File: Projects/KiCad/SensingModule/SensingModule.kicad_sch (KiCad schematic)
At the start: 18 parts, among them J1 Conn_01x04_Pin, J2 Conn_01x04_Socket, J3 Micro_SD_Card_Det_Hirose_DM3AT, U1 NUCLEO-F303K8, U2 MCP2562-E-P, U3 24LC256

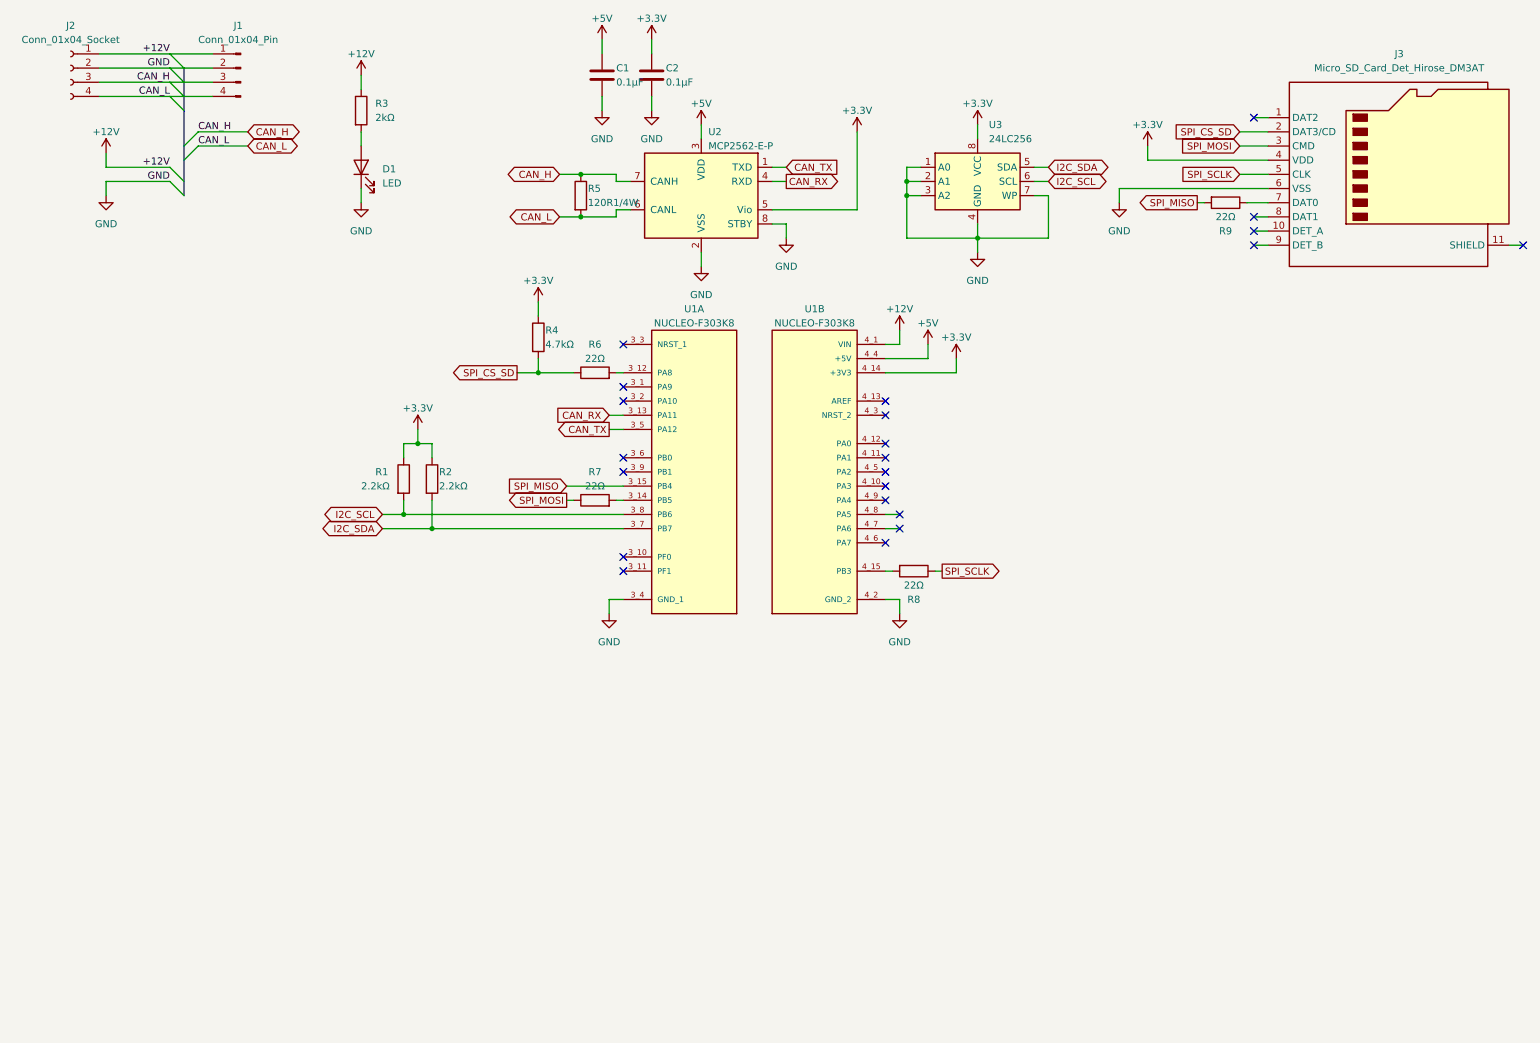
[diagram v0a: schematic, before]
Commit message: 通信モジュールを一旦作成
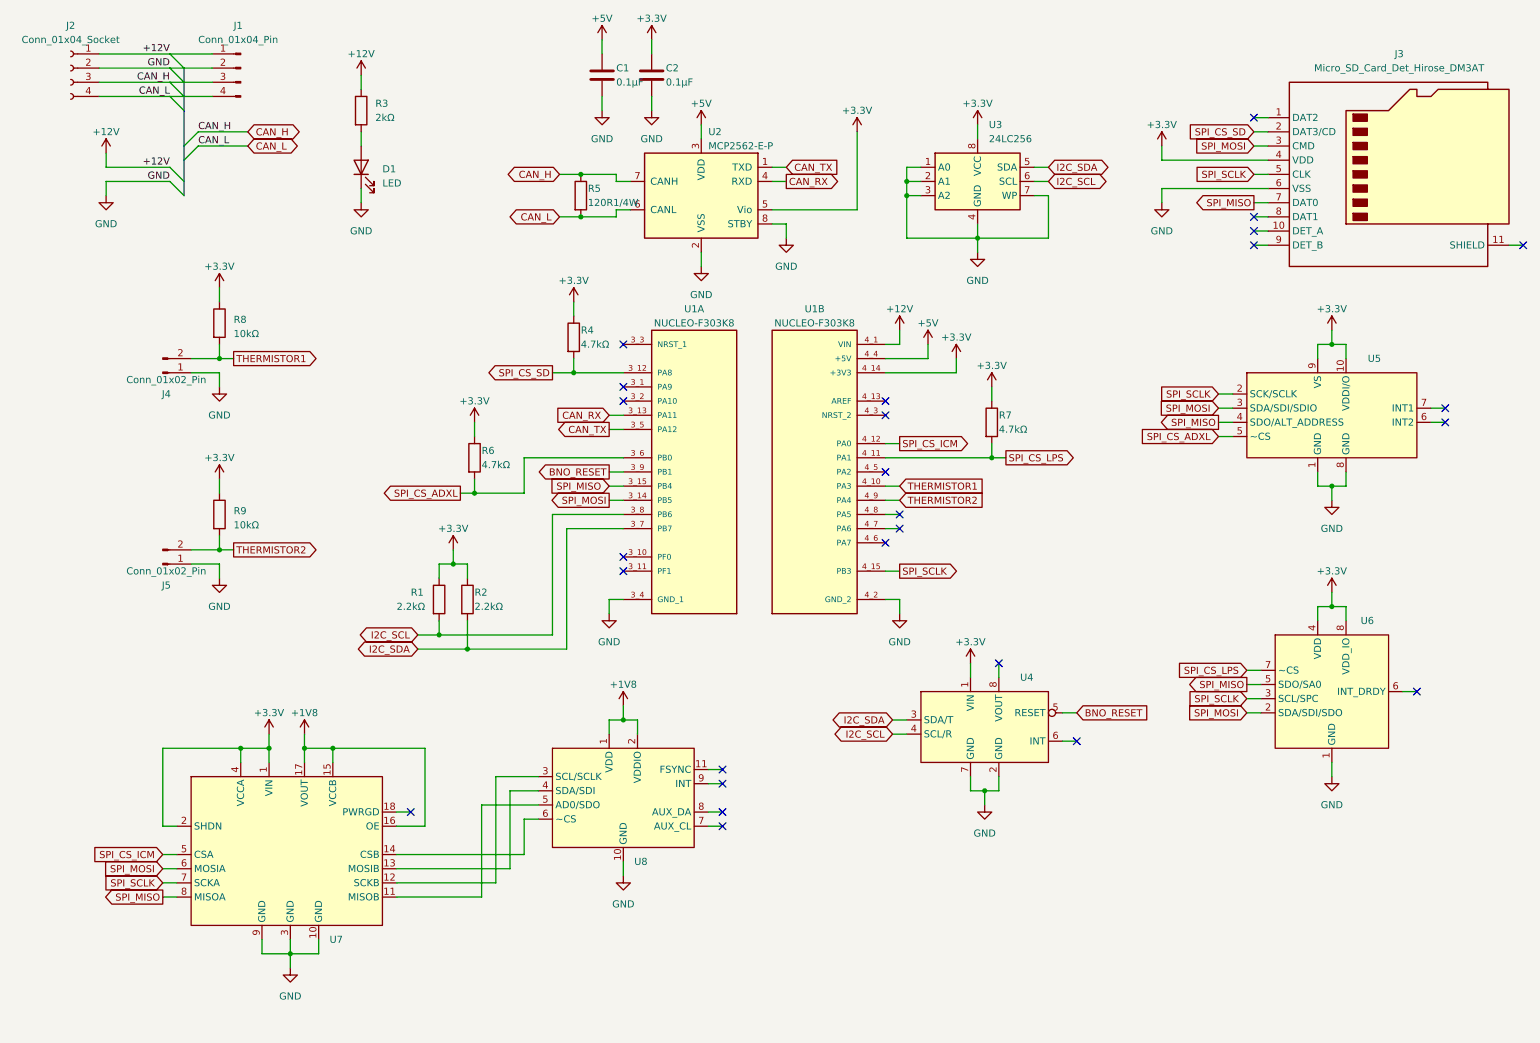
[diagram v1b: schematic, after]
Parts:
- added J4, J5: Conn_01x02_Pin, Hirose_Connector:Hirose_DF1B, symbol Connector:Conn_01x02_Pin
- added U4: ~, Akizuki_BNO055_Module:BNO055, symbol Akizuki_BNO055_Module:BNO055
- added U5: ~, StrawberryLinux_ADXL375_Module:ADXL375, symbol StrawberryLinux_ADXL375_Module:ADXL375
- added U6: ~, StrawberryLinux_LPS33HW_Module:LPS33HW, symbol StrawberryLinux_LPS33HW_Module:LPS33HW
- added U7: ~, StrawberryLinux_TUX0304_Module:TUX0304, symbol StrawberryLinux_TUX0304_Module:TUX0304
- added U8: ~, StrawberryLinux_ICM20948_Module:ICM20948, symbol StrawberryLinux_ICM20948_Module:ICM20948
- R6, R7: value 22Ω -> 4.7kΩ
- R8, R9: value 22Ω -> 10kΩ
- U1: footprint MODULE_NUCLEO-F303K8 -> NUCLEO-F303K8:MODULE_NUCLEO-F303K8
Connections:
- net +3.3V: now also R6.1, R7.1, R8.1, R9.1, U4.1 (VIN), U5.10 (VDDI/O), U5.9 (VS), U6.4 (VDD), U6.8 (VDD_IO), U7.1 (VIN), U7.2 (SHDN), U7.4 (VCCA)
- net GND: now also J4.1 (Pin_1), J5.1 (Pin_1), U4.2 (GND), U4.7 (GND), U5.1 (GND), U5.8 (GND), U6.1 (GND), U7.10 (GND), U7.3 (GND), U7.9 (GND), U8.10 (GND)
- net I2C_SCL: now also U4.4 (SCL/R)
- net I2C_SDA: now also U4.3 (SDA/T)
- net SPI_CS_SD: now also U1.3_12 (PA8); no longer R6.1
- net SPI_MISO: now also J3.7 (DAT0), U5.4 (SDO/ALT_ADDRESS), U6.5 (SDO/SA0), U7.8 (MISOA); no longer R9.2
- net SPI_MOSI: now also U1.3_14 (PB5), U5.3 (SDA/SDI/SDIO), U6.2 (SDA/SDI/SDO), U7.6 (MOSIA); no longer R7.1
- net SPI_SCLK: now also U1.4_15 (PB3), U5.2 (SCK/SCLK), U6.3 (SCL/SPC), U7.7 (SCKA); no longer R8.1
- net SPI_CS_ADXL: now reaches R6.2
- net SPI_CS_ADXL: now also U1.3_6 (PB0), U5.5 (~CS); no longer U1.3_12 (PA8)
- net THERMISTOR1: now reaches R8.2
- net THERMISTOR1: now also U1.4_10 (PA3), J4.2 (Pin_2); no longer U1.4_15 (PB3)
- net SPI_CS_LPS: now reaches R7.2
- net SPI_CS_LPS: now also U1.4_11 (PA1), U6.7 (~CS); no longer U1.3_14 (PB5)
- net SPI_CS_ICM: now reaches U1.4_12 (PA0)
- net SPI_CS_ICM: now also U7.5 (CSA)
- net THERMISTOR2: now reaches U1.4_9 (PA4)
- net THERMISTOR2: now also R9.2, J5.2 (Pin_2)
- net BNO_RESET: now reaches U1.3_9 (PB1)
- net BNO_RESET: now also U4.5 (RESET)
- new net: U7.12 (SCKB), U8.3 (SCL/SCLK)
- new net: U7.13 (MOSIB), U8.4 (SDA/SDI)
- new net: U7.11 (MISOB), U8.5 (AD0/SDO)
- new net: U7.14 (CSB), U8.6 (~CS)
- new net +1V8: U7.15 (VCCB), U7.16 (OE), U7.17 (VOUT), U8.1 (VDD), U8.2 (VDDIO)
- no-connect marks 22 -> 26
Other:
- moved on the sheet: R1, R2, R4

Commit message: フライトモジュールのKiCadを追加
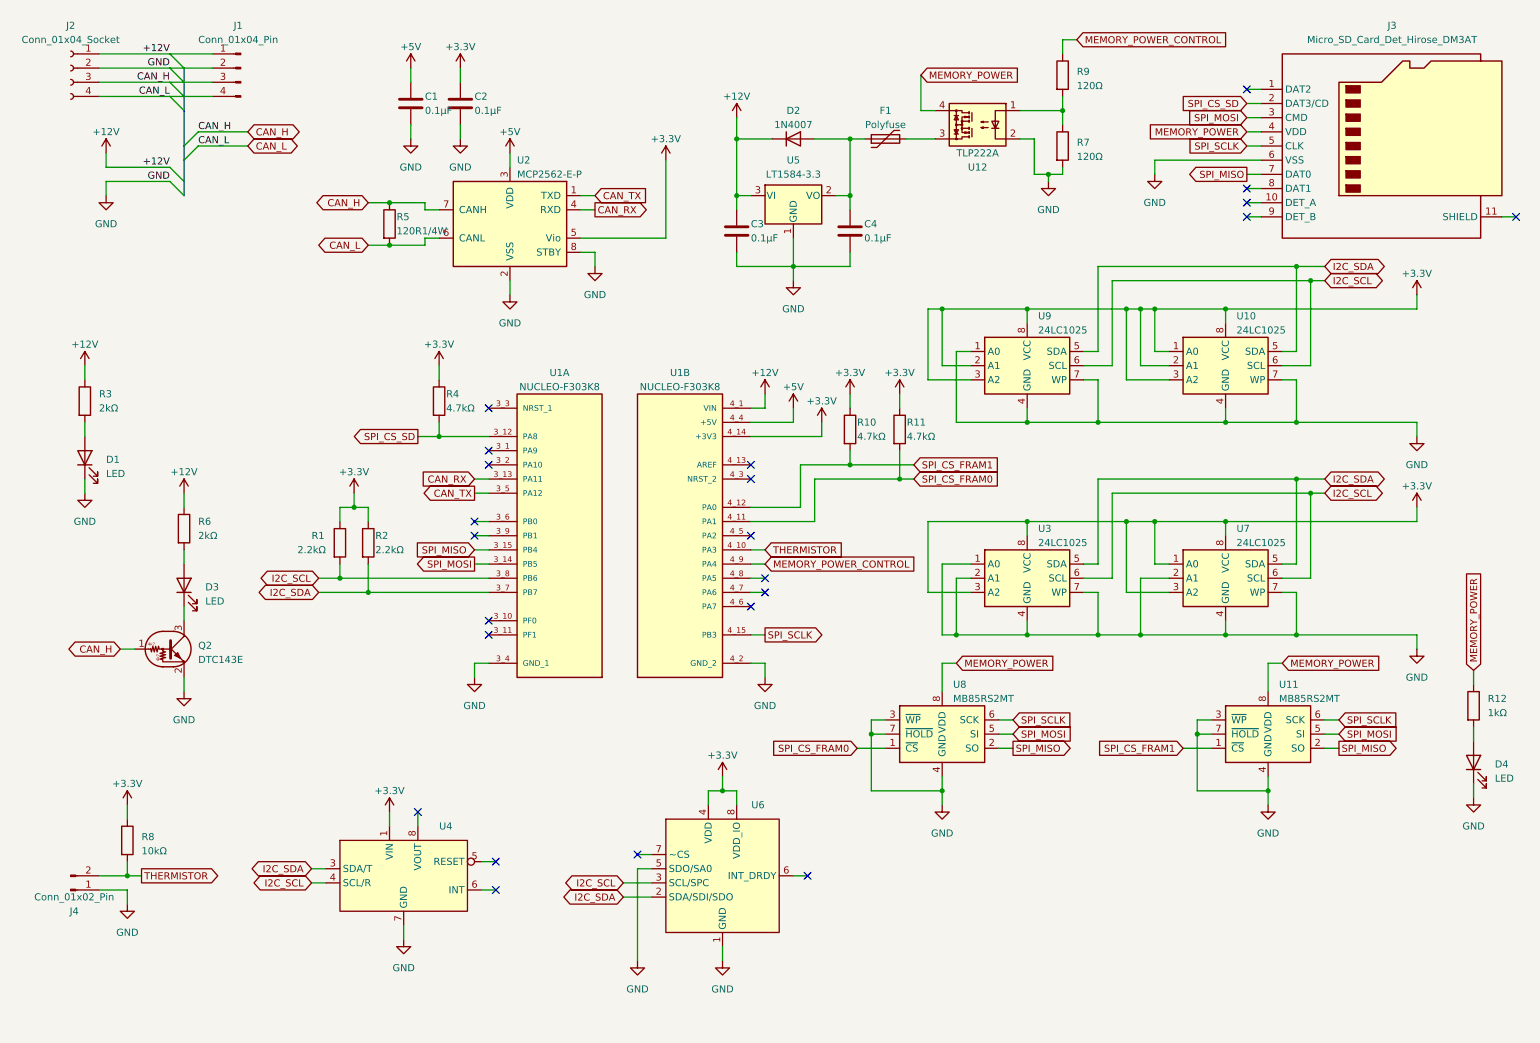
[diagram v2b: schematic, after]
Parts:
- removed J5: Conn_01x02_Pin, Hirose_Connector:Hirose_DF1B, symbol Connector:Conn_01x02_Pin
- removed U3: 24LC256, Package_DIP:DIP-8_W7.62mm, symbol Memory_EEPROM:24LC256
- removed U5: ~, StrawberryLinux_ADXL375_Module:ADXL375, symbol StrawberryLinux_ADXL375_Module:ADXL375
- removed U7: ~, StrawberryLinux_TUX0304_Module:TUX0304, symbol StrawberryLinux_TUX0304_Module:TUX0304
- removed U8: ~, StrawberryLinux_ICM20948_Module:ICM20948, symbol StrawberryLinux_ICM20948_Module:ICM20948
- added C3, C4: 0.1μF, Capacitor_SMD:C_0805_2012Metric_Pad1.18x1.45mm_HandSolder, symbol Device:C
- added D2: 1N4007, Diode_THT:D_DO-41_SOD81_P10.16mm_Horizontal, symbol Diode:1N4007
- added D3, D4: LED, LED_SMD:LED_1206_3216Metric_Pad1.42x1.75mm_HandSolder, symbol Device:LED
- added F1: Polyfuse, Fuse:Fuse_BelFuse_0ZRE0005FF_L8.3mm_W3.8mm, symbol Device:Polyfuse
- added Q2: DTC143E, Package_TO_SOT_THT:TO-92_Inline, symbol Transistor_BJT:DTC143E
- added R10, R11: 4.7kΩ, Resistor_SMD:R_0805_2012Metric_Pad1.20x1.40mm_HandSolder, symbol Device:R
- added R12: 1kΩ, Resistor_SMD:R_0805_2012Metric_Pad1.20x1.40mm_HandSolder, symbol Device:R
- added U10, U3, U7, U9: 24LC1025, Package_DIP:DIP-8_W7.62mm, symbol Memory_EEPROM:24LC1025
- added U11, U8: MB85RS2MT, Package_DIP:DIP-8_W7.62mm, symbol Memory_NVRAM:MB85RS2MT
- added U12: TLP222A, Package_DIP:DIP-4_W7.62mm, symbol Relay_SolidState:TLP222A
- added U5: LT1584-3.3, Package_TO_SOT_THT:TO-220-3_Vertical, symbol Regulator_Linear:LT1584-3.3
- R6: value 4.7kΩ -> 2kΩ
- R7: value 4.7kΩ -> 120Ω
- R9: value 10kΩ -> 120Ω
- U1: footprint NUCLEO-F303K8:MODULE_NUCLEO-F303K8 -> MODULE_NUCLEO-F303K8
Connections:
- net +12V: now also R6.1, C3.1, D2.1 (K), U5.3 (VI)
- net +3.3V: now also R10.1, R11.1, U10.1 (A0), U10.2 (A1), U10.3 (A2), U10.8 (VCC), U3.3 (A2), U3.8 (VCC), U7.1 (A0), U7.3 (A2), U7.8 (VCC), U9.2 (A1), U9.3 (A2), U9.8 (VCC); no longer J3.4 (VDD), R6.1, R7.1, R9.1
- net CAN_H: now also Q2.1 (B)
- net GND: now also R7.2, U6.5 (SDO/SA0), C3.2, C4.2, D4.1 (K), Q2.2 (E), U10.4 (GND), U10.7 (WP), U11.3 (~{WP}), U11.4 (GND), U11.7 (~{HOLD}), U12.2, U3.1 (A0), U3.2 (A1), U3.4 (GND), U3.7 (WP), U5.1 (GND), U7.2 (A1), U7.4 (GND), U7.7 (WP), U8.3 (~{WP}), U8.4 (GND), U8.7 (~{HOLD}), U9.1 (A0), U9.4 (GND), U9.7 (WP); no longer U4.2 (GND)
- net I2C_SCL: now also U6.3 (SCL/SPC), U10.6 (SCL), U3.6 (SCL), U7.6 (SCL), U9.6 (SCL)
- net I2C_SDA: now also U6.2 (SDA/SDI/SDO), U10.5 (SDA), U3.5 (SDA), U7.5 (SDA), U9.5 (SDA)
- net SPI_MISO: now also U11.2 (SO), U8.2 (SO); no longer U6.5 (SDO/SA0)
- net SPI_MOSI: now also U11.5 (SI), U8.5 (SI); no longer U6.2 (SDA/SDI/SDO)
- net SPI_SCLK: now also U11.6 (SCK), U8.6 (SCK); no longer U6.3 (SCL/SPC)
- net BNO_RESET: no longer names the net of U4.5 (RESET)
- net BNO_RESET: no longer U1.3_9 (PB1)
- net SPI_CS_ADXL: no longer names the net of R6.2
- net SPI_CS_ADXL: now also D3.2 (A); no longer U1.3_6 (PB0)
- net SPI_CS_ICM renamed SPI_CS_FRAM1
- net SPI_CS_FRAM1: now also R10.2, U11.1 (~{CS})
- removed net SPI_CS_LPS: R7.2, U1.4_11 (PA1), U6.7 (~CS)
- net THERMISTOR1 renamed THERMISTOR
- net THERMISTOR2: no longer names the net of R9.2
- net THERMISTOR2: now also R7.1, U12.1; no longer U1.4_9 (PA4)
- new net: D3.1 (K), Q2.3 (C)
- new net: D4.2 (A), R12.2
- new net: C4.1, D2.2 (A), F1.1, U5.2 (VO)
- new net: F1.2, U12.3
- new net MEMORY_POWER: J3.4 (VDD), R12.1, U11.8 (VDD), U12.4, U8.8 (VDD)
- new net MEMORY_POWER_CONTROL: R9.1, U1.4_9 (PA4)
- new net SPI_CS_FRAM0: R11.2, U1.4_11 (PA1), U8.1 (~{CS})
- no-connect marks 26 -> 23
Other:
- moved on the sheet: C1, C2, D1, J3, J4, R1, R2, R3, R4, R5, R8, U1A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

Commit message: バスパワーの接続を修正
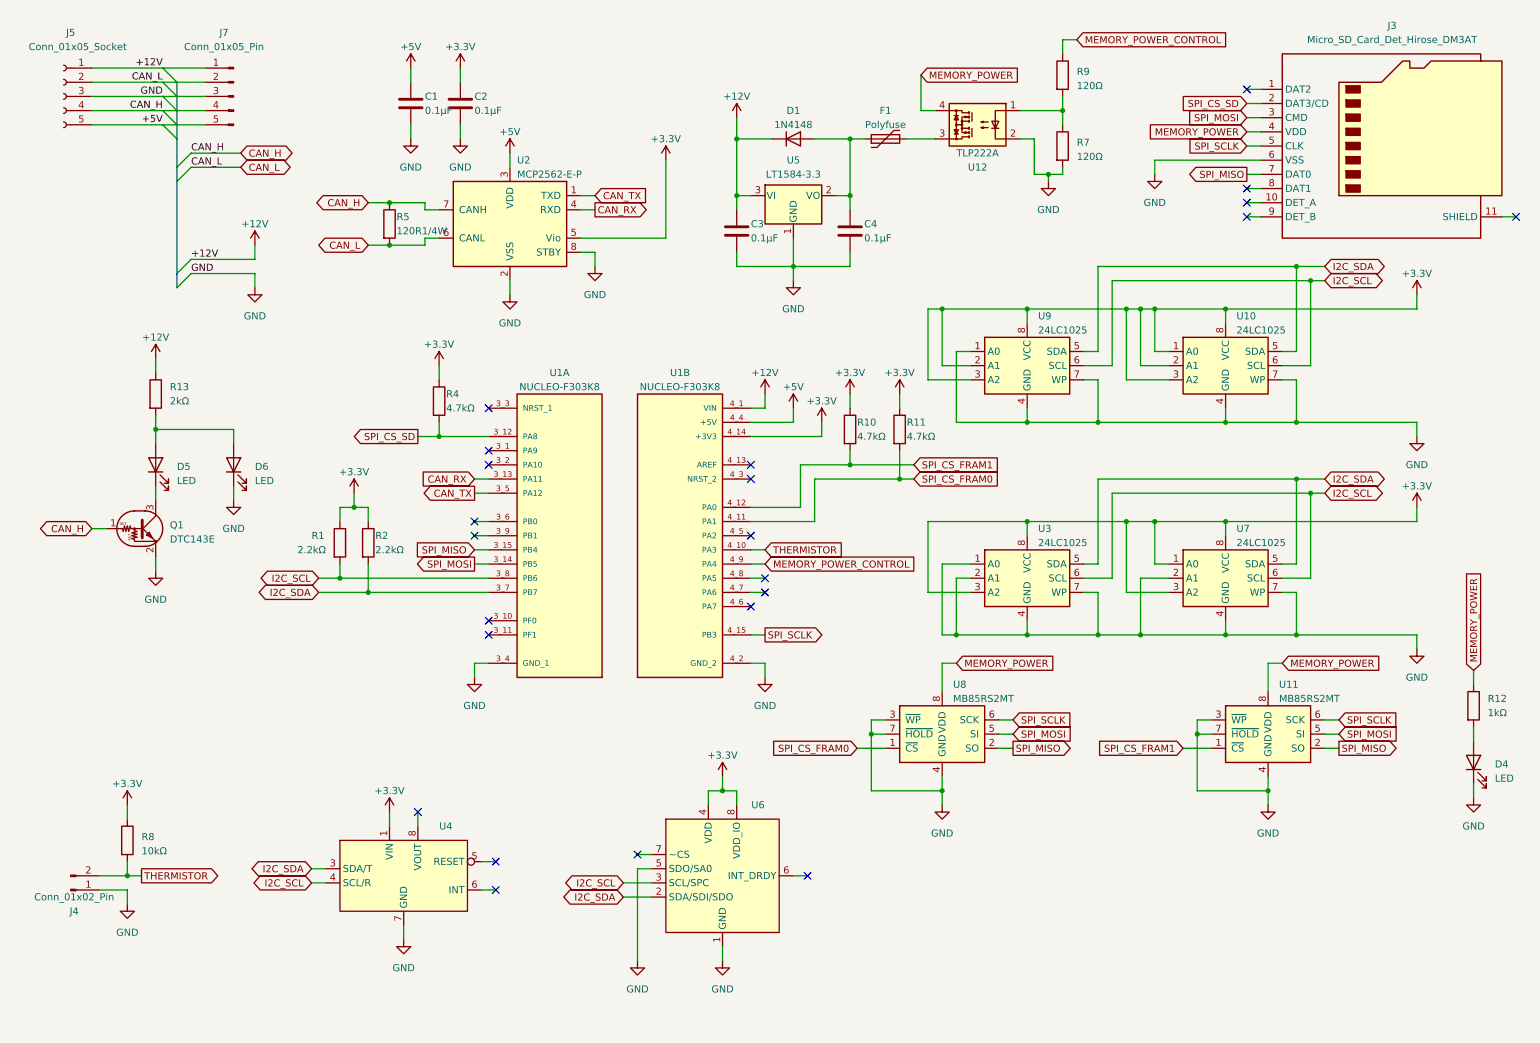
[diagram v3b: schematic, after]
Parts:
- removed D1, D3: LED, LED_SMD:LED_1206_3216Metric_Pad1.42x1.75mm_HandSolder, symbol Device:LED
- removed D2: 1N4007, Diode_THT:D_DO-41_SOD81_P10.16mm_Horizontal, symbol Diode:1N4007
- removed J1: Conn_01x04_Pin, Connector_PinHeader_1.27mm:PinHeader_1x04_P1.27mm_Vertical, symbol Connector:Conn_01x04_Pin
- removed J2: Conn_01x04_Socket, Connector_PinSocket_1.27mm:PinSocket_1x04_P1.27mm_Vertical, symbol Connector:Conn_01x04_Socket
- removed Q2: DTC143E, Package_TO_SOT_THT:TO-92_Inline, symbol Transistor_BJT:DTC143E
- removed R3, R6: 2kΩ, Resistor_SMD:R_0805_2012Metric_Pad1.20x1.40mm_HandSolder, symbol Device:R
- added D1: 1N4148, Diode_THT:D_DO-35_SOD27_P7.62mm_Horizontal, symbol Diode:1N4148
- added D5, D6: LED, LED_SMD:LED_1206_3216Metric_Pad1.42x1.75mm_HandSolder, symbol Device:LED
- added J5: Conn_01x05_Socket, Connector_PinSocket_2.54mm:PinSocket_1x05_P2.54mm_Vertical, symbol Connector:Conn_01x05_Socket
- added J7: Conn_01x05_Pin, Connector_PinHeader_2.54mm:PinHeader_1x05_P2.54mm_Vertical, symbol Connector:Conn_01x05_Pin
- added Q1: DTC143E, Package_TO_SOT_THT:TO-92_Inline, symbol Transistor_BJT:DTC143E
- added R13: 2kΩ, Resistor_SMD:R_0805_2012Metric_Pad1.20x1.40mm_HandSolder, symbol Device:R
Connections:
- net +12V: now also D1.1 (K), J5.1 (Pin_1), J7.1 (Pin_1), R13.1
- net +5V: now also J5.5 (Pin_5), J7.5 (Pin_5)
- net CAN_H: now also J5.4 (Pin_4), J7.4 (Pin_4), Q1.1 (B)
- net CAN_L: now also J5.2 (Pin_2), J7.2 (Pin_2)
- net GND: now also D6.1 (K), J5.3 (Pin_3), J7.3 (Pin_3), Q1.2 (E)
- net at C4.1, F1.1, U5.2 (VO): now also D1.2 (A)
- new net: D5.2 (A), D6.2 (A), R13.2
- new net: D5.1 (K), Q1.3 (C)
